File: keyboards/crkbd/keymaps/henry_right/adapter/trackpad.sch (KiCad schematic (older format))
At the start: 10 parts, among them U1 Elite-C, U2 ProMicro

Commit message: 수정중
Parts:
- gave numbers to parts that had none: 7
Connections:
- net MAP_B3C7 is gone; now on net MAP_B3F1: U1.28 (F1)
- net TP_DR is gone; now on net LVL_SHIFT: U1.25 (B7)
- net +3V3: now also J1.1 (Pin_1)
- net GND: now also J1.2 (Pin_2), U4.7 (GND)
- net MISO_3V3: now also J1.11 (Pin_11)
- net MOSI_3V3: now also J1.8 (Pin_8)
- net PB6: now also J1.9 (Pin_9)
- net SCK_3V3: now also J1.12 (Pin_12)
- net TP_CS_3V3: now also J1.10 (Pin_10)
- no-connect marks 0 -> 8
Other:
- moved on the sheet: J1
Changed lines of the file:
@@
 Wire Wire Line
 	5800 1450 6100 1450
-Text GLabel 2750 3100 3    50   Input ~ 0
-TP_DR
+Text GLabel 3800 2550 3    50   Input ~ 0
+TP_DR_3V3
 Wire Wire Line
 	2750 3100 2750 2950
@@
 	1950 1450 2250 1450
 Text GLabel 3050 3100 3    50   Input ~ 0
-MAP_B3C7
+MAP_B3F1
 Wire Wire Line
 	3050 3100 3050 2950
@@
 	7500 2450 7800 2450
 $Comp
-L Logic_LevelTranslator:TXB0104D U?
+L Logic_LevelTranslator:TXB0104D U4
 U 1 1 5D4E5066
 P 5200 4950
-F 0 "U?" H 5200 4161 50  0000 C CNN
+F 0 "U4" H 5200 4161 50  0000 C CNN
 F 1 "TXB0104D" H 5200 4070 50  0000 C CNN
 F 2 "Package_SO:SOIC-14_3.9x8.7mm_P1.27mm" H 5200 4200 50  0001 C CNN
@@
 $EndComp
 $Comp
-L Regulator_Linear:NCP1117-3.3_SOT223 U?
+L Regulator_Linear:NCP1117-3.3_SOT223 U3
 U 1 1 5D4E82C1
 P 2400 4450
-F 0 "U?" H 2400 4692 50  0000 C CNN
+F 0 "U3" H 2400 4692 50  0000 C CNN
 F 1 "NCP1117-3.3_SOT223" H 2400 4601 50  0000 C CNN
 F 2 "Package_TO_SOT_SMD:SOT-223-3_TabPin2" H 2400 4650 50  0001 C CNN
@@
 $EndComp
 $Comp
-L Device:C_Small C?
+L Device:C_Small C1
 U 1 1 5D4F60AD
 P 1950 4750
-F 0 "C?" H 2042 4796 50  0000 L CNN
+F 0 "C1" H 2042 4796 50  0000 L CNN
 F 1 "10uF" H 2042 4705 50  0000 L CNN
 F 2 "Capacitor_SMD:C_0805_2012Metric" H 1950 4750 50  0001 C CNN
@@
 $EndComp
 $Comp
-L Device:C_Small C?
+L Device:C_Small C2
 U 1 1 5D502666
 P 2850 4750
-F 0 "C?" H 2942 4796 50  0000 L CNN
+F 0 "C2" H 2942 4796 50  0000 L CNN
 F 1 "10uF" H 2942 4705 50  0000 L CNN
 F 2 "Capacitor_SMD:C_0805_2012Metric" H 2850 4750 50  0001 C CNN
@@
 $EndComp
 $Comp
-L power:+3.3V #PWR?
+L power:+3.3V #PWR01
 U 1 1 5D519034
 P 3050 4450
-F 0 "#PWR?" H 3050 4300 50  0001 C CNN
+F 0 "#PWR01" H 3050 4300 50  0001 C CNN
 F 1 "+3.3V" V 3065 4578 50  0000 L CNN
 F 2 "" H 3050 4450 50  0001 C CNN
@@
 $EndComp
 $Comp
-L power:+3.3V #PWR?
+L power:+3.3V #PWR04
 U 1 1 5D5345C8
 P 5100 3900
-F 0 "#PWR?" H 5100 3750 50  0001 C CNN
-F 1 "+3.3V" H 5115 4073 50  0000 C CNN
+F 0 "#PWR04" H 5100 3750 50  0001 C CNN
+F 1 "+3.3V" V 5115 4073 50  0000 C CNN
 F 2 "" H 5100 3900 50  0001 C CNN
 F 3 "" H 5100 3900 50  0001 C CNN
@@
 $EndComp
 $Comp
-L power:+5V #PWR?
+L power:+5V #PWR05
 U 1 1 5D536D5D
 P 5300 3900
-F 0 "#PWR?" H 5300 3750 50  0001 C CNN
+F 0 "#PWR05" H 5300 3750 50  0001 C CNN
 F 1 "+5V" V 5315 4028 50  0000 L CNN
 F 2 "" H 5300 3900 50  0001 C CNN
@@
 $EndComp
 $Comp
-L Device:C_Small C?
+L Device:C_Small C4
 U 1 1 5D5377AE
 P 5500 4000
-F 0 "C?" H 5592 4046 50  0000 L CNN
+F 0 "C4" H 5592 4046 50  0000 L CNN
 F 1 "100nF" H 5592 3955 50  0000 L CNN
 F 2 "Capacitor_SMD:C_0805_2012Metric" H 5500 4000 50  0001 C CNN
@@
 $EndComp
 $Comp
-L Device:C_Small C?
+L Device:C_Small C3
 U 1 1 5D5387B2
 P 4900 4000
-F 0 "C?" H 4992 4046 50  0000 L CNN
+F 0 "C3" H 4992 4046 50  0000 L CNN
 F 1 "100nF" H 4992 3955 50  0000 L CNN
 F 2 "Capacitor_SMD:C_0805_2012Metric" H 4900 4000 50  0001 C CNN
@@
 $EndComp
 $Comp
-L power:GND #PWR?
+L power:GND #PWR06
 U 1 1 5D539FF6
 P 5500 4100
-F 0 "#PWR?" H 5500 3850 50  0001 C CNN
+F 0 "#PWR06" H 5500 3850 50  0001 C CNN
 F 1 "GND" H 5505 3927 50  0000 C CNN
 F 2 "" H 5500 4100 50  0001 C CNN
@@
 $EndComp
 $Comp
-L power:GND #PWR?
+L power:GND #PWR03
 U 1 1 5D53A4E3
 P 4900 4100
-F 0 "#PWR?" H 4900 3850 50  0001 C CNN
+F 0 "#PWR03" H 4900 3850 50  0001 C CNN
 F 1 "GND" H 4905 3927 50  0000 C CNN
 F 2 "" H 4900 4100 50  0001 C CNN
@@
 	4800 4450 4650 4450
 $Comp
-L power:GND #PWR?
+L power:GND #PWR02
 U 1 1 5D565A2C
 P 4450 4450
-F 0 "#PWR?" H 4450 4200 50  0001 C CNN
+F 0 "#PWR02" H 4450 4200 50  0001 C CNN
 F 1 "GND" H 4455 4277 50  0000 C CNN
 F 2 "" H 4450 4450 50  0001 C CNN
@@
 Connection ~ 4650 4450
 $Comp
-L Connector_Generic:Conn_01x12 J?
+L power:GND #PWR0108
+U 1 1 5D4A1B9F
+P 7400 4500
+F 0 "#PWR0108" H 7400 4250 50  0001 C CNN
+F 1 "GND" V 7405 4327 50  0000 C CNN
+F 2 "" H 7400 4500 50  0001 C CNN
+F 3 "" H 7400 4500 50  0001 C CNN
+	1    7400 4500
+	0    -1   -1   0
+$EndComp
+$Comp
+L power:+3.3V #PWR0112
+U 1 1 5D4A230C
+P 7400 4400
+F 0 "#PWR0112" H 7400 4250 50  0001 C CNN
+F 1 "+3.3V" V 7415 4573 50  0000 C CNN
+F 2 "" H 7400 4400 50  0001 C CNN
+F 3 "" H 7400 4400 50  0001 C CNN
+	1    7400 4400
+	0    1    1    0
+$EndComp
+$Comp
+L Connector_Generic:Conn_01x12 J1
 U 1 1 5D572BD5
 P 7200 4900
-F 0 "J?" H 7118 4075 50  0000 C CNN
+F 0 "J1" H 7118 4075 50  0000 C CNN
 F 1 "Conn_01x12" H 7118 4166 50  0000 C CNN
 F 2 "Connector_FFC-FPC:Hirose_FH12-12S-0.5SH_1x12-1MP_P0.50mm_Horizontal" H 7118 4167 50  0001 C CNN
 F 3 "~" H 7200 4900 50  0001 C CNN
 	1    7200 4900
-	-1   0    0    1
+	-1   0    0    -1
+$EndComp
+Text GLabel 7400 5500 2    50   Input ~ 0
+SCK_3V3
+Text GLabel 7400 5400 2    50   Input ~ 0
+MISO_3V3
+Text GLabel 7400 5300 2    50   Input ~ 0
+TP_CS_3V3
+Text GLabel 7400 5100 2    50   Input ~ 0
+MOSI_3V3
+Text GLabel 7400 5200 2    50   Input ~ 0
+TP_DR_3V3
+Text GLabel 7550 4900 2    50   Input ~ 0
+TP_BTN3_3V3
+Text GLabel 7550 5000 2    50   Input ~ 0
+TP_BTN2_3V3
+Text GLabel 7550 4800 2    50   Input ~ 0
+TP_BTN1_3V3
+Text GLabel 2750 3100 3    50   Input ~ 0
+LVL_SHIFT
+NoConn ~ 7400 4600
+NoConn ~ 7400 4700
+NoConn ~ 7400 4800
+NoConn ~ 7400 4900
+NoConn ~ 7400 5000
+NoConn ~ 7550 5000
+NoConn ~ 7550 4900
+NoConn ~ 7550 4800
+$Comp
+L power:GND #PWR0113
+U 1 1 5D4BD70B
+P 5200 5650
+F 0 "#PWR0113" H 5200 5400 50  0001 C CNN
+F 1 "GND" H 5205 5477 50  0000 C CNN
+F 2 "" H 5200 5650 50  0001 C CNN
+F 3 "" H 5200 5650 50  0001 C CNN
+	1    5200 5650
+	0    1    1    0
 $EndComp
 $EndSCHEMATC

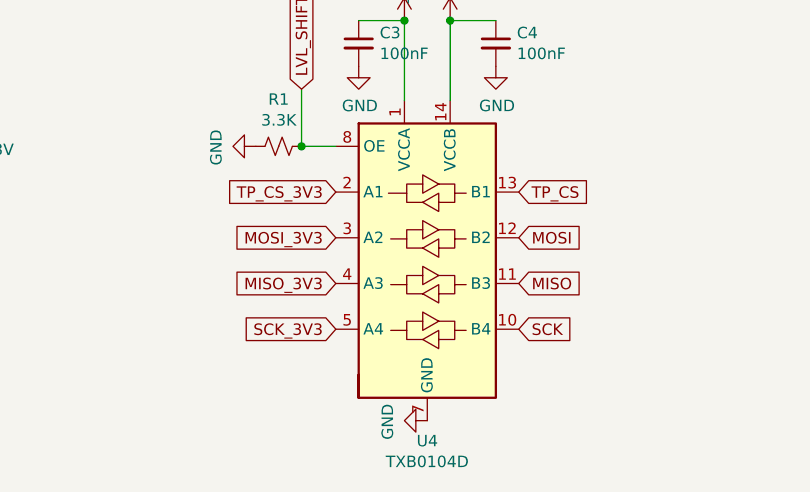
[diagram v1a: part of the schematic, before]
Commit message: 배치 거의 끝난듯
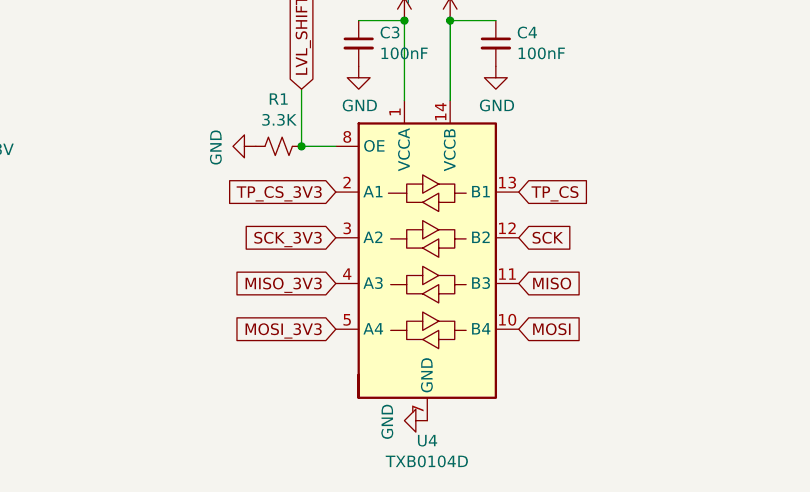
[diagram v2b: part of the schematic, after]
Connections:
- net MOSI: now also U4.10 (B4); no longer U4.12 (B2)
- net MOSI_3V3: now also U4.5 (A4); no longer U4.3 (A2)
- net SCK: now also U4.12 (B2); no longer U4.10 (B4)
- net SCK_3V3: now also U4.3 (A2); no longer U4.5 (A4)
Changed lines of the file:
@@
 Text GLabel 5600 4650 2    50   Input ~ 0
 TP_CS
-Text GLabel 5600 4850 2    50   Input ~ 0
+Text GLabel 5600 5250 2    50   Input ~ 0
 MOSI
 Text GLabel 5600 5050 2    50   Input ~ 0
 MISO
-Text GLabel 5600 5250 2    50   Input ~ 0
+Text GLabel 5600 4850 2    50   Input ~ 0
 SCK
-Text GLabel 4800 5250 0    50   Input ~ 0
+Text GLabel 4800 4850 0    50   Input ~ 0
 SCK_3V3
 Text GLabel 4800 5050 0    50   Input ~ 0
 MISO_3V3
-Text GLabel 4800 4850 0    50   Input ~ 0
+Text GLabel 4800 5250 0    50   Input ~ 0
 MOSI_3V3
 Text GLabel 4800 4650 0    50   Input ~ 0

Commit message: drc통과
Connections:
- net PB6: no longer J1.9 (Pin_9)
- net PD2: now also J1.9 (Pin_9)
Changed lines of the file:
@@
 Wire Wire Line
 	5800 1450 6100 1450
-Text GLabel 3800 2550 3    50   Input ~ 0
+Text GLabel 2200 1550 3    50   Input ~ 0
 TP_DR_3V3
 Wire Wire Line

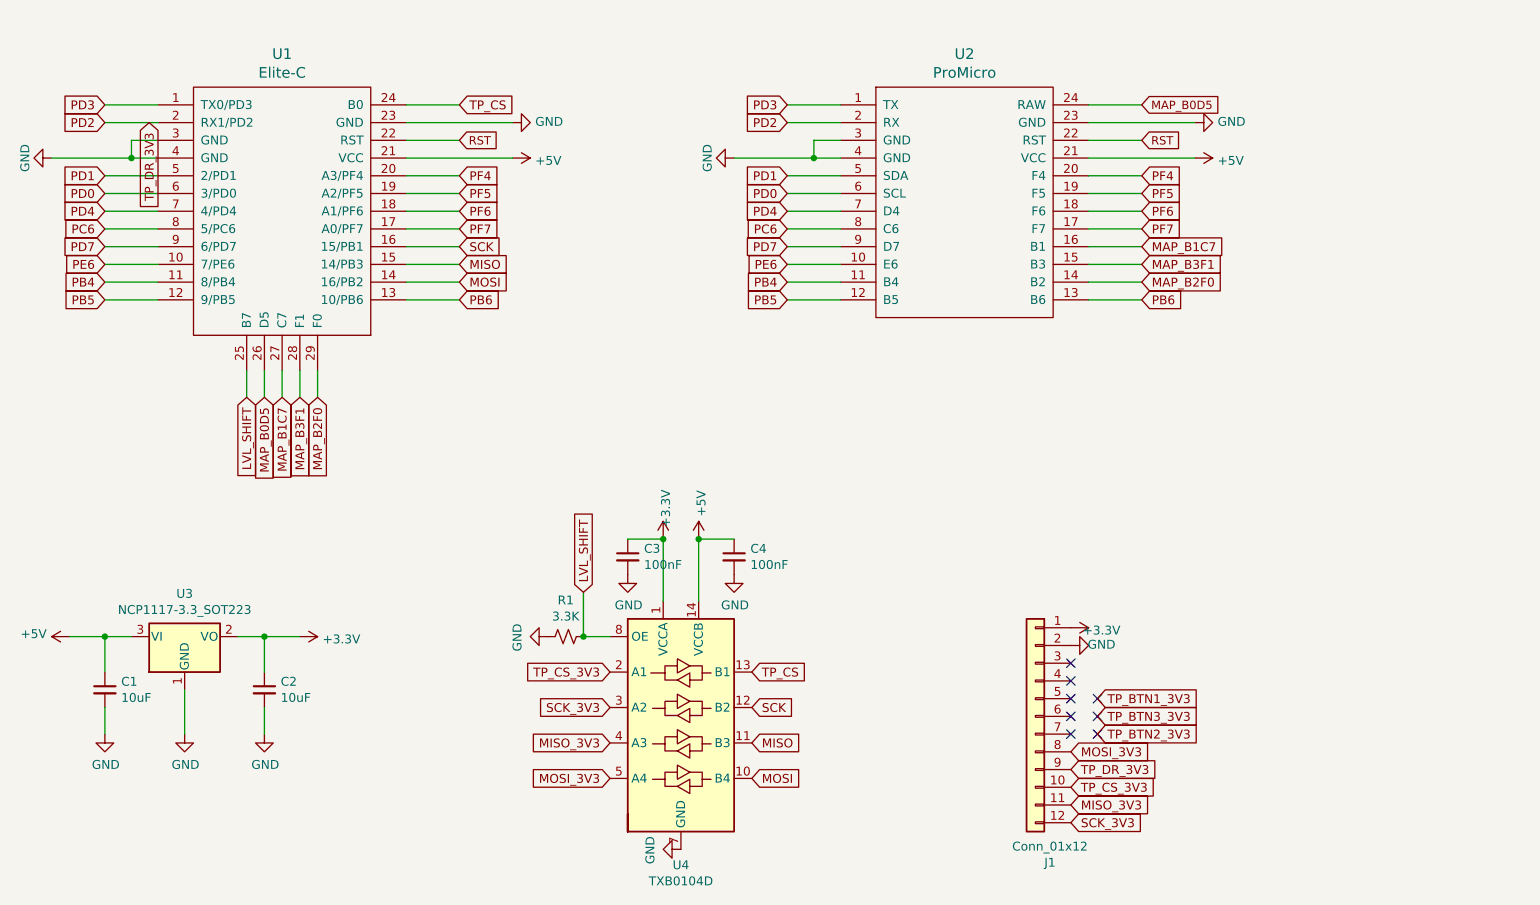
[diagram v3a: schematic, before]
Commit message: i2c로 변경중
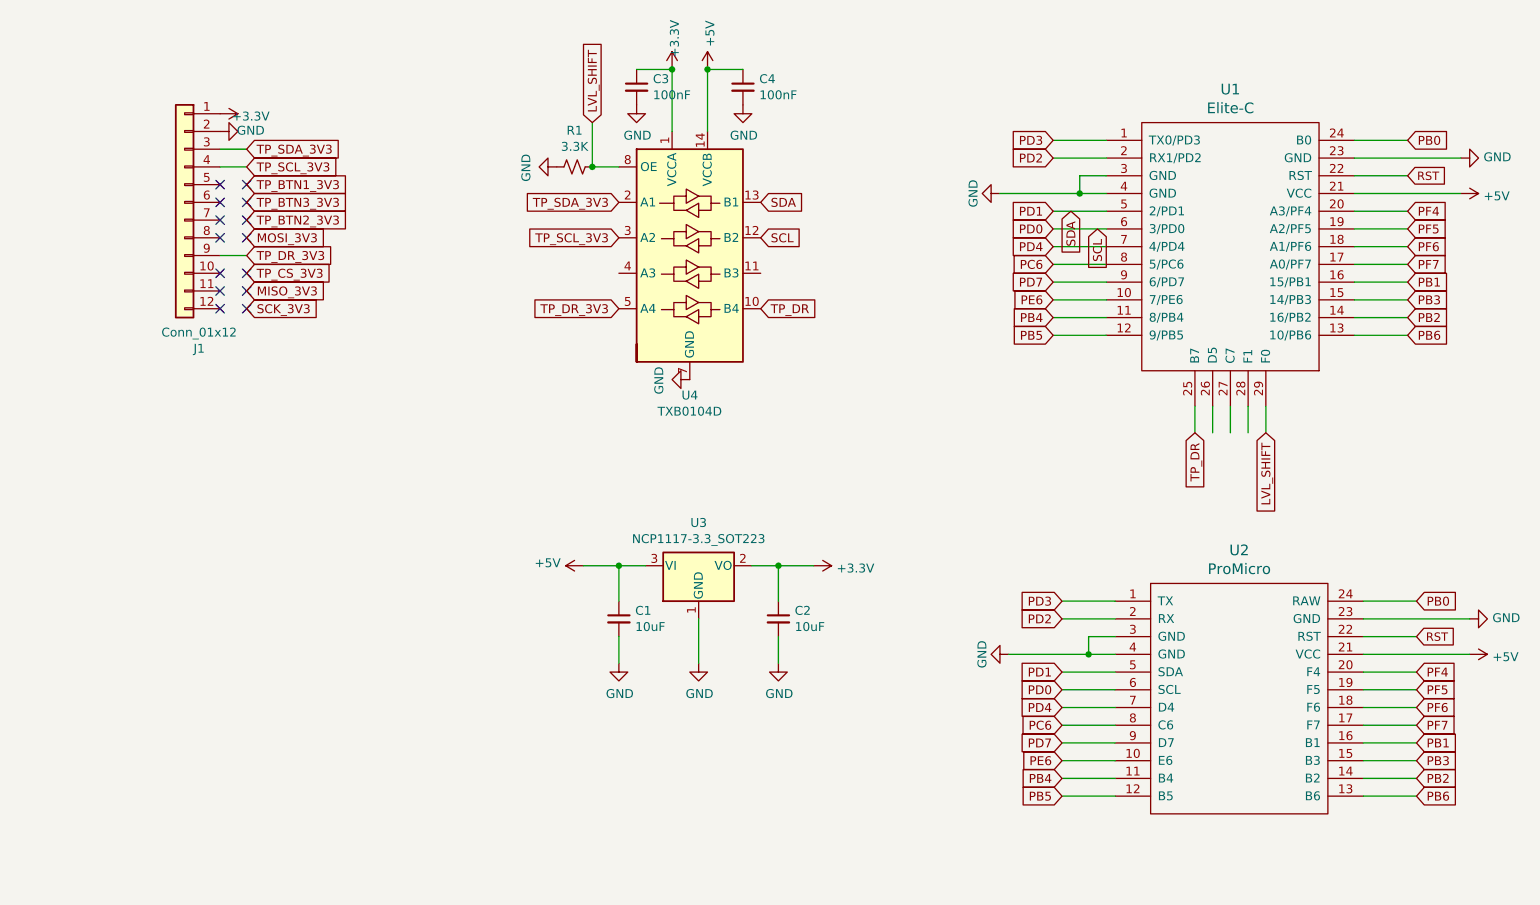
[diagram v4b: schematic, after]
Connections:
- net labels added: PB0, PB1, PB2, PB3, SCL, SDA, TP_DR, TP_SCL_3V3, TP_SDA_3V3
- net labels removed: MAP_B0D5, MAP_B1C7, MAP_B2F0, MAP_B3F1, MISO, MOSI, SCK, TP_CS
- wire segments 72 -> 75
- no-connect marks 8 -> 14
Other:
- moved on the sheet: C1, C2, C3, C4, J1, R1, U1, U2, U3, U4

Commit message: 최소구성요소
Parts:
- removed U2: ProMicro, trackpad:ArduinoProMicro, symbol trackpad-rescue:corne-classic-rescue_ProMicro-kbd-corne-classic-cache-trackpad-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
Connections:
- wire segments 75 -> 49
- no-connect marks 14 -> 17
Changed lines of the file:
@@
 $EndDescr
-$Comp
-L trackpad-rescue:corne-classic-rescue_ProMicro-kbd-corne-classic-cache-trackpad-rescue U2
-U 1 1 5BF8BB0A
-P 8350 5000
-F 0 "U2" H 8350 6037 60  0000 C CNN
-F 1 "ProMicro" H 8350 5931 60  0000 C CNN
-F 2 "trackpad:ArduinoProMicro" H 8450 3950 60  0001 C CNN
-F 3 "" H 8450 3950 60  0000 C CNN
-	1    8350 5000
-	1    0    0    -1
-$EndComp
 $Comp
 L trackpad-rescue:Elite-C-keebio-trackpad-rescue U1
@@
 $EndComp
 $Comp
-L power:GND #PWR0101
-U 1 1 5BFB3888
-P 7050 4550
-F 0 "#PWR0101" H 7050 4300 50  0001 C CNN
-F 1 "GND" H 7050 4400 50  0000 C CNN
-F 2 "" H 7050 4550 50  0001 C CNN
-F 3 "" H 7050 4550 50  0001 C CNN
-	1    7050 4550
-	0    1    1    0
-$EndComp
-Wire Wire Line
-	7050 4550 7500 4550
-$Comp
-L power:GND #PWR0102
-U 1 1 5BFC66DA
-P 9650 4350
-F 0 "#PWR0102" H 9650 4100 50  0001 C CNN
-F 1 "GND" V 9655 4222 50  0000 R CNN
-F 2 "" H 9650 4350 50  0001 C CNN
-F 3 "" H 9650 4350 50  0001 C CNN
-	1    9650 4350
-	0    -1   -1   0
-$EndComp
-$Comp
-L power:+5V #PWR0103
-U 1 1 5BFC7635
-P 9650 4550
-F 0 "#PWR0103" H 9650 4400 50  0001 C CNN
-F 1 "+5V" V 9665 4678 50  0000 L CNN
-F 2 "" H 9650 4550 50  0001 C CNN
-F 3 "" H 9650 4550 50  0001 C CNN
-	1    9650 4550
-	0    1    1    0
-$EndComp
-Wire Wire Line
-	7650 4450 7500 4450
-Connection ~ 7500 4550
-Wire Wire Line
-	7500 4550 7650 4550
-Wire Wire Line
-	7500 4450 7500 4550
-Text GLabel 9350 4450 2    47   Input ~ 0
-RST
-Text GLabel 7350 4350 0    50   Input ~ 0
-PD2
-Wire Wire Line
-	7350 4350 7650 4350
-Wire Wire Line
-	9050 4350 9650 4350
-Wire Wire Line
-	9050 4450 9350 4450
-Wire Wire Line
-	9050 4550 9650 4550
-Text GLabel 7350 4650 0    50   Input ~ 0
-PD1
-Wire Wire Line
-	7350 4650 7650 4650
-Text GLabel 7350 4750 0    50   Input ~ 0
-PD0
-Wire Wire Line
-	7350 4750 7650 4750
-Text GLabel 7350 4850 0    50   Input ~ 0
-PD4
-Wire Wire Line
-	7350 4850 7650 4850
-Text GLabel 7350 4950 0    50   Input ~ 0
-PC6
-Wire Wire Line
-	7350 4950 7650 4950
-Text GLabel 7350 5050 0    50   Input ~ 0
-PD7
-Wire Wire Line
-	7350 5050 7650 5050
-Text GLabel 7350 5150 0    50   Input ~ 0
-PE6
-Wire Wire Line
-	7350 5150 7650 5150
-$Comp
 L power:GND #PWR0104
 U 1 1 5BFDDB09
@@
 Wire Wire Line
 	7300 2750 7600 2750
-Wire Wire Line
-	9350 5350 9050 5350
-Wire Wire Line
-	9350 5150 9050 5150
-Wire Wire Line
-	9350 5050 9050 5050
-Text GLabel 9350 4950 2    50   Input ~ 0
-PF7
-Wire Wire Line
-	9350 4950 9050 4950
-Text GLabel 9350 4850 2    50   Input ~ 0
-PF6
-Wire Wire Line
-	9350 4850 9050 4850
-Text GLabel 9350 4750 2    50   Input ~ 0
-PF5
-Wire Wire Line
-	9350 4750 9050 4750
-Text GLabel 9350 4650 2    50   Input ~ 0
-PF4
-Wire Wire Line
-	9350 4650 9050 4650
-Text GLabel 9350 5350 2    50   Input ~ 0
-PB6
-Text GLabel 7350 4250 0    50   Input ~ 0
-PD3
-Wire Wire Line
-	7350 4250 7650 4250
 Wire Wire Line
 	8100 3300 8100 3150
@@
 Wire Wire Line
 	8200 3300 8200 3150
-Text GLabel 7350 5250 0    50   Input ~ 0
-PB4
-Wire Wire Line
-	7350 5250 7650 5250
 Wire Wire Line
 	8300 3300 8300 3150
@@
 Text GLabel 4700 1550 1    50   Input ~ 0
 LVL_SHIFT
-Text GLabel 7350 5350 0    50   Input ~ 0
-PB5
-Wire Wire Line
-	7350 5350 7650 5350
-Wire Wire Line
-	9050 4250 9350 4250
-Wire Wire Line
-	9050 5250 9350 5250
 $Comp
 L Logic_LevelTranslator:TXB0104D U4
@@
 Text GLabel 9300 1650 2    50   Input ~ 0
 PB0
-Text GLabel 9350 4250 2    50   Input ~ 0
-PB0
 Text GLabel 9300 2450 2    50   Input ~ 0
 PB1
@@
 PB3
 Text GLabel 9300 2650 2    50   Input ~ 0
-PB2
-Text GLabel 9350 5050 2    50   Input ~ 0
-PB1
-Text GLabel 9350 5150 2    50   Input ~ 0
-PB3
-Text GLabel 9350 5250 2    50   Input ~ 0
 PB2
 Text GLabel 2750 1700 2    50   Input ~ 0
@@
 Wire Wire Line
 	2600 2300 2750 2300
+NoConn ~ 8200 3300
+NoConn ~ 8300 3300
+NoConn ~ 8400 3300
 $EndSCHEMATC

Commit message: 아트웍 시작 전.
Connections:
- net LVL_SHIFT: now also U1.27 (C7); no longer U1.29 (F0)
- net TP_BTN1_3V3: now also J1.5 (Pin_5), U4.4 (A3)
- net TP_BTN1: now reaches U4.11 (B3)
- net TP_BTN1: now also U1.29 (F0)
- no-connect marks 17 -> 14
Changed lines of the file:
@@
 EESchema Schematic File Version 4
 LIBS:trackpad-cache
-EELAYER 26 0
+EELAYER 29 0
 EELAYER END
 $Descr A4 11693 8268
@@
 Text GLabel 2750 1900 2    50   Input ~ 0
 TP_BTN1_3V3
-Text GLabel 8500 3300 3    50   Input ~ 0
+Text GLabel 8300 3300 3    50   Input ~ 0
 LVL_SHIFT
-NoConn ~ 2600 1900
 NoConn ~ 2600 2000
 NoConn ~ 2600 2100
 NoConn ~ 2750 2100
 NoConn ~ 2750 2000
-NoConn ~ 2750 1900
 $Comp
 L power:GND #PWR0113
@@
 	2600 2300 2750 2300
 NoConn ~ 8200 3300
-NoConn ~ 8300 3300
 NoConn ~ 8400 3300
+Text GLabel 4850 2400 0    50   Input ~ 0
+TP_BTN1_3V3
+Text GLabel 5650 2400 2    50   Input ~ 0
+TP_BTN1
+Text GLabel 8500 3300 3    50   Input ~ 0
+TP_BTN1
+Wire Wire Line
+	2600 1900 2750 1900
 $EndSCHEMATC

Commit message: 배치 변경
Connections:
- net LVL_SHIFT: now also U1.29 (F0); no longer U1.27 (C7)
- net PD0: now also U4.11 (B3); no longer U4.12 (B2)
- net PD1: now also U4.10 (B4); no longer U4.13 (B1)
- net TP_BTN1: now also U1.27 (C7), U4.12 (B2); no longer U1.29 (F0), U4.11 (B3)
- net TP_BTN1_3V3: now also U4.3 (A2); no longer U4.4 (A3)
- net TP_DR: now also U4.13 (B1); no longer U4.10 (B4)
- net TP_DR_3V3: now also U4.2 (A1); no longer U4.5 (A4)
- net TP_SCL_3V3: now also U4.4 (A3); no longer U4.3 (A2)
- net TP_SDA_3V3: now also U4.5 (A4); no longer U4.2 (A1)
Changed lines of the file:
@@
 	5350 1250 5550 1250
 Connection ~ 5350 1250
-Text GLabel 5650 2000 2    50   Input ~ 0
+Text GLabel 5650 2600 2    50   Input ~ 0
 SDA
-Text GLabel 5650 2200 2    50   Input ~ 0
+Text GLabel 5650 2400 2    50   Input ~ 0
 SCL
 Wire Wire Line
@@
 Text GLabel 2750 1900 2    50   Input ~ 0
 TP_BTN1_3V3
-Text GLabel 8300 3300 3    50   Input ~ 0
+Text GLabel 8500 3300 3    50   Input ~ 0
 LVL_SHIFT
 NoConn ~ 2600 2000
@@
 Text GLabel 2750 1800 2    50   Input ~ 0
 TP_SCL_3V3
+Text GLabel 4850 2600 0    50   Input ~ 0
+TP_SDA_3V3
+Text GLabel 4850 2400 0    50   Input ~ 0
+TP_SCL_3V3
 Text GLabel 4850 2000 0    50   Input ~ 0
-TP_SDA_3V3
-Text GLabel 4850 2200 0    50   Input ~ 0
-TP_SCL_3V3
-Text GLabel 4850 2600 0    50   Input ~ 0
 TP_DR_3V3
-Text GLabel 5650 2600 2    50   Input ~ 0
+Text GLabel 5650 2000 2    50   Input ~ 0
 TP_DR
 Text GLabel 7400 2050 3    50   Input ~ 0
@@
 NoConn ~ 8200 3300
 NoConn ~ 8400 3300
-Text GLabel 4850 2400 0    50   Input ~ 0
+Text GLabel 4850 2200 0    50   Input ~ 0
 TP_BTN1_3V3
-Text GLabel 5650 2400 2    50   Input ~ 0
+Text GLabel 5650 2200 2    50   Input ~ 0
 TP_BTN1
-Text GLabel 8500 3300 3    50   Input ~ 0
+Text GLabel 8300 3300 3    50   Input ~ 0
 TP_BTN1
 Wire Wire Line
